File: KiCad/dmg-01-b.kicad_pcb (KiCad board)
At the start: 2 copper layers, 83 x 78.5 mm, 64 parts, among them CN1 SCREEN, CN2 CART, CN3 EXT, P1 GND PAD, P2 GND PAD, P3 GND PAD, P4 GND PAD, SW1 POWER_SW, U1 CPU, U2 VRAM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

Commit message: add images
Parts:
- G1: moved to F.Cu
- moved G1 32.7 mm to (38.3, 60.0), turned to 0 degrees
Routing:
- net GND: vias 138 -> 142
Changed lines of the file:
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@@
     )
   )
+  (footprint "eda-glyphs:kmc" (layer "F.Cu")
+    (at 38.3 60)
+    (property "Sheetfile" "dmg-01-b.kicad_sch")
+    (property "Sheetname" "")
+    (attr board_only exclude_from_pos_files)
+    (fp_text reference "G1" (at -0.254 -3.81) (layer "F.SilkS") hide
+      (effects (font (size 1.524 1.524) (thickness 0.3)))
+    )
+    (fp_text value "kmc" (at 0.75 0) (layer "F.SilkS") hide
+      (effects (font (size 1.524 1.524) (thickness 0.3)))
+    )
+    (fp_poly (pts
+        (xy -1.560389 -1.873672)
+        (xy -1.247107 -1.873672)
+        (xy -1.247107 -1.560389)
+        (xy -0.939849 -1.560389)
+        (xy -0.939849 -2.186954)
+        (xy -0.620541 -2.186954)
+        (xy -0.620541 -1.873672)
+        (xy -0.313283 -1.873672)
+        (xy -0.313283 -1.560389)
+        (xy 0 -1.560389)
+        (xy 0 -1.247106)
+        (xy 0.626565 -1.247106)
+        (xy 0.626565 -0.939848)
+        (xy 1.253131 -0.939848)
+        (xy 1.253131 -0.626566)
+        (xy 1.560389 -0.626566)
+        (xy 1.560389 -0.313283)
+        (xy 1.873671 -0.313283)
+        (xy 1.873671 0)
+        (xy 2.180929 0)
+        (xy 2.180929 -0.626566)
+        (xy 2.500237 -0.626566)
+        (xy 2.500237 0.006025)
+        (xy 2.186954 0.006025)
+        (xy 2.186954 0.319307)
+        (xy 1.873671 0.319307)
+        (xy 1.873671 0.939848)
+        (xy 1.566413 0.939848)
+        (xy 1.566413 2.186954)
+        (xy 1.247106 2.186954)
+        (xy 1.247106 1.879696)
+        (xy 0.933823 1.879696)
+        (xy 0.933823 1.566414)
+        (xy 0.626565 1.566414)
+        (xy 0.626565 2.186954)
+        (xy 0.307258 2.186954)
+        (xy 0.307258 1.879696)
+        (xy -0.006025 1.879696)
+        (xy -0.006025 1.566414)
+        (xy -0.620541 1.566414)
+        (xy -0.620541 1.879696)
+        (xy -0.933824 1.879696)
+        (xy -0.933824 2.186954)
+        (xy -1.253131 2.186954)
+        (xy -1.253131 1.566414)
+        (xy -1.560389 1.566414)
+        (xy -1.560389 1.879696)
+        (xy -1.879697 1.879696)
+        (xy -1.879697 0.626565)
+        (xy -2.186955 0.626565)
+        (xy -2.186955 0.319307)
+        (xy -2.500237 0.319307)
+        (xy -2.500237 -0.626566)
+        (xy -2.186955 -0.626566)
+        (xy -1.873672 -0.626566)
+        (xy -1.566414 -0.626566)
+        (xy -0.933824 -0.626566)
+        (xy -0.626566 -0.626566)
+        (xy -0.626566 -0.933824)
+        (xy -0.933824 -0.933824)
+        (xy -0.933824 -0.626566)
+        (xy -1.566414 -0.626566)
+        (xy -1.566414 -0.933824)
+        (xy -1.873672 -0.933824)
+        (xy -1.873672 -0.626566)
+        (xy -2.186955 -0.626566)
+        (xy -2.186955 -1.247106)
+        (xy -1.879697 -1.247106)
+        (xy -1.879697 -2.186954)
+        (xy -1.560389 -2.186954)
+      ) (layer "F.SilkS") (width 0) (fill solid))
+  )
   (footprint "Capacitor_SMD:C_0805_2012Metric_Pad1.18x1.45mm_HandSolder" (layer "F.Cu")
     (at 70 66.5)
@@
       (net 113 "-BATT") (pinfunction "BAT-") (pintype "passive"))
   )
-  (footprint "eda-glyphs:kmc" (layer "B.Cu")
-    (at 70.6 65.2 180)
-    (property "Sheetfile" "dmg-01-b.kicad_sch")
-    (property "Sheetname" "")
-    (attr board_only exclude_from_pos_files)
-    (fp_text reference "G1" (at -0.254 3.81) (layer "B.SilkS") hide
-      (effects (font (size 1.524 1.524) (thickness 0.3)) (justify mirror))
-    )
-    (fp_text value "kmc" (at 0.75 0) (layer "B.SilkS") hide
-      (effects (font (size 1.524 1.524) (thickness 0.3)) (justify mirror))
-    )
-    (fp_poly (pts
-        (xy -1.560389 1.873672)
-        (xy -1.247107 1.873672)
-        (xy -1.247107 1.560389)
-        (xy -0.939849 1.560389)
-        (xy -0.939849 2.186954)
-        (xy -0.620541 2.186954)
-        (xy -0.620541 1.873672)
-        (xy -0.313283 1.873672)
-        (xy -0.313283 1.560389)
-        (xy 0 1.560389)
-        (xy 0 1.247106)
-        (xy 0.626565 1.247106)
-        (xy 0.626565 0.939848)
-        (xy 1.253131 0.939848)
-        (xy 1.253131 0.626566)
-        (xy 1.560389 0.626566)
-        (xy 1.560389 0.313283)
-        (xy 1.873671 0.313283)
-        (xy 1.873671 0)
-        (xy 2.180929 0)
-        (xy 2.180929 0.626566)
-        (xy 2.500237 0.626566)
-        (xy 2.500237 -0.006025)
-        (xy 2.186954 -0.006025)
-        (xy 2.186954 -0.319307)
-        (xy 1.873671 -0.319307)
-        (xy 1.873671 -0.939848)
-        (xy 1.566413 -0.939848)
-        (xy 1.566413 -2.186954)
-        (xy 1.247106 -2.186954)
-        (xy 1.247106 -1.879696)
-        (xy 0.933823 -1.879696)
-        (xy 0.933823 -1.566414)
-        (xy 0.626565 -1.566414)
-        (xy 0.626565 -2.186954)
-        (xy 0.307258 -2.186954)
-        (xy 0.307258 -1.879696)
-        (xy -0.006025 -1.879696)
-        (xy -0.006025 -1.566414)
-        (xy -0.620541 -1.566414)
-        (xy -0.620541 -1.879696)
-        (xy -0.933824 -1.879696)
-        (xy -0.933824 -2.186954)
-        (xy -1.253131 -2.186954)
-        (xy -1.253131 -1.566414)
-        (xy -1.560389 -1.566414)
-        (xy -1.560389 -1.879696)
-        (xy -1.879697 -1.879696)
-        (xy -1.879697 -0.626565)
-        (xy -2.186955 -0.626565)
-        (xy -2.186955 -0.319307)
-        (xy -2.500237 -0.319307)
-        (xy -2.500237 0.626566)
-        (xy -2.186955 0.626566)
-        (xy -1.873672 0.626566)
-        (xy -1.566414 0.626566)
-        (xy -0.933824 0.626566)
-        (xy -0.626566 0.626566)
-        (xy -0.626566 0.933824)
-        (xy -0.933824 0.933824)
-        (xy -0.933824 0.626566)
-        (xy -1.566414 0.626566)
-        (xy -1.566414 0.933824)
-        (xy -1.873672 0.933824)
-        (xy -1.873672 0.626566)
-        (xy -2.186955 0.626566)
-        (xy -2.186955 1.247106)
-        (xy -1.879697 1.247106)
-        (xy -1.879697 2.186954)
-        (xy -1.560389 2.186954)
-      ) (layer "B.SilkS") (width 0) (fill solid))
-  )
   (footprint "kmc_lib:2.54_PAD_SMD_X7" (layer "B.Cu")
     (at 80.01 96.808 180)
@@
   (via (at 99.5 98) (size 0.8) (drill 0.4) (layers "F.Cu" "B.Cu") (free) (net 4))
   (via locked (at 64.5 95) (size 0.8) (drill 0.4) (layers "F.Cu" "B.Cu") (free) (net 4))
+  (via (at 44.5 59.5) (size 0.8) (drill 0.4) (layers "F.Cu" "B.Cu") (free) (net 4))
   (via (at 48.5 47.5) (size 0.8) (drill 0.4) (layers "F.Cu" "B.Cu") (free) (net 4))
   (via (at 93 46) (size 0.8) (drill 0.4) (layers "F.Cu" "B.Cu") (free) (net 4))
@@
   (via (at 58 53.3) (size 0.8) (drill 0.4) (layers "F.Cu" "B.Cu") (free) (net 4))
   (via (at 46.5 32.6) (size 0.8) (drill 0.4) (layers "F.Cu" "B.Cu") (free) (net 4))
+  (via (at 32 58) (size 0.8) (drill 0.4) (layers "F.Cu" "B.Cu") (free) (net 4))
   (via (at 66 41.2) (size 0.8) (drill 0.4) (layers "F.Cu" "B.Cu") (free) (net 4))
   (via locked (at 84 95) (size 0.8) (drill 0.4) (layers "F.Cu" "B.Cu") (free) (net 4))
@@
   (via locked (at 76.5 95) (size 0.8) (drill 0.4) (layers "F.Cu" "B.Cu") (free) (net 4))
   (via (at 60.3 36.3) (size 0.8) (drill 0.4) (layers "F.Cu" "B.Cu") (free) (net 4))
+  (via (at 32 62) (size 0.8) (drill 0.4) (layers "F.Cu" "B.Cu") (free) (net 4))
   (via (at 61.1 73.123522) (size 0.8) (drill 0.4) (layers "F.Cu" "B.Cu") (free) (net 4))
   (via locked (at 90 95) (size 0.8) (drill 0.4) (layers "F.Cu" "B.Cu") (free) (net 4))
@@
   (via (at 35.5 32.6) (size 0.8) (drill 0.4) (layers "F.Cu" "B.Cu") (free) (net 4))
   (via (at 62 49.2) (size 0.8) (drill 0.4) (layers "F.Cu" "B.Cu") (free) (net 4))
+  (via (at 44.5 63) (size 0.8) (drill 0.4) (layers "F.Cu" "B.Cu") (free) (net 4))
   (via (at 109 65) (size 0.8) (drill 0.4) (layers "F.Cu" "B.Cu") (free) (net 4))
   (via locked (at 87 95) (size 0.8) (drill 0.4) (layers "F.Cu" "B.Cu") (free) (net 4))
@@
     )
   )
-  (group "" (id ccebfcd8-a1f0-4a8e-b077-2c83658638a7)
-    (members
-      81ec17ae-7d6d-4574-af35-d4487429f438
-      8b992f09-a688-4516-ad0c-980240b33cef
-      cd2f768b-c470-48a2-84e0-481a100e3a25
-      eae9265d-2640-47e1-b8fe-024c47af79a6
-    )
-  )

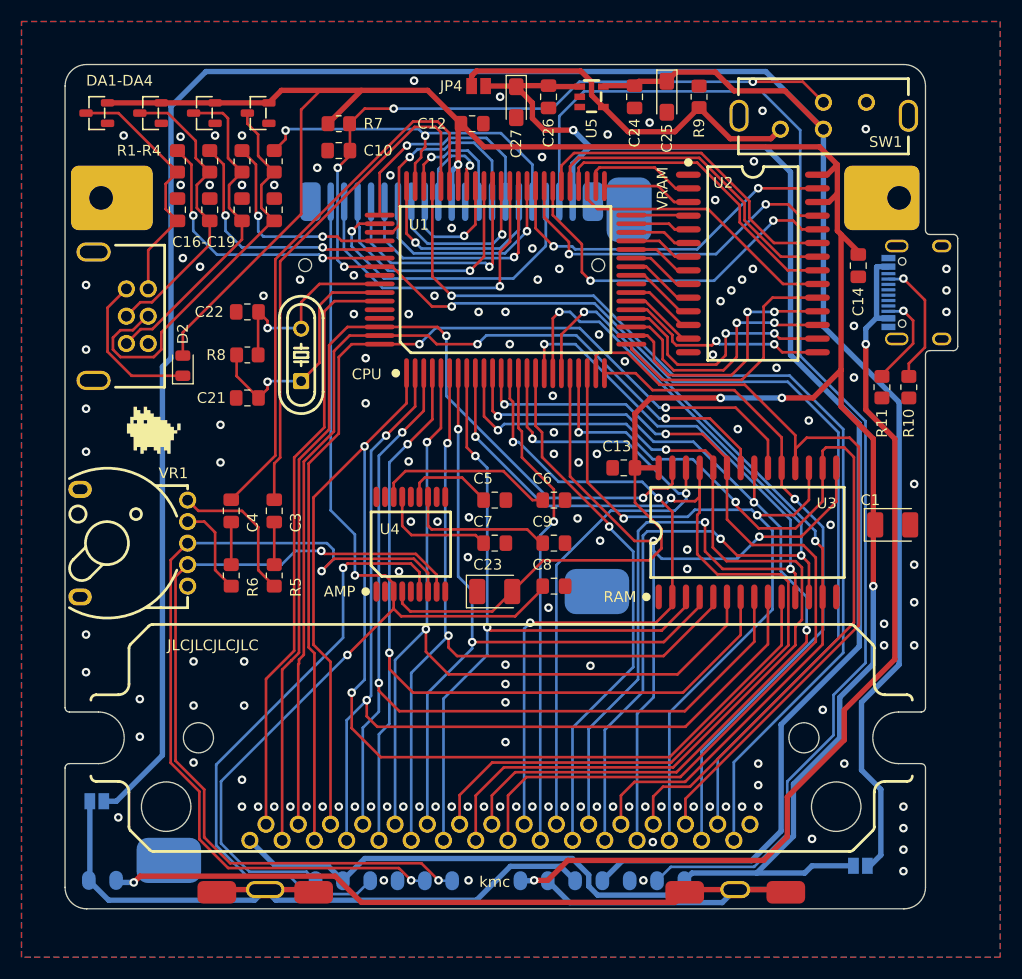
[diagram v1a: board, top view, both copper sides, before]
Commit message: - fix c23 orientation - fix d2 footprint - minor silkscreen changes
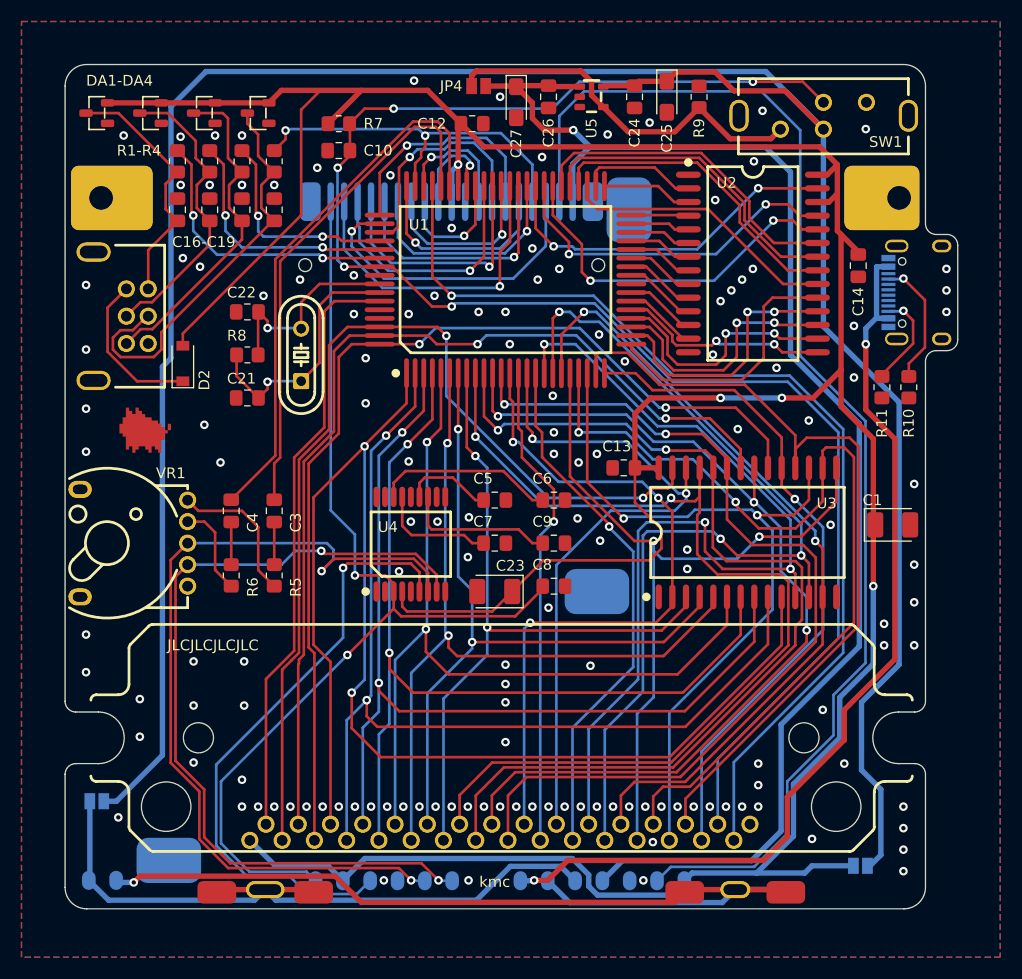
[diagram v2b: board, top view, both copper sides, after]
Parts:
- C23: value 100uf -> 100µf
- D2: value CD4148W -> 1N414; footprint Diode_SMD:D_0805_2012Metric -> Diode_SMD:D_SOD-123
- U5: footprint easyeda2kicad:SOT-23-5_L2.9-W1.6-P0.95-LS2.8-BL -> kmc_lib:SOT-23-5_L2.9-W1.6-P0.95-LS2.8-BL
- moved G1 0.58 mm to (37.8, 59.7)
- moved D2 0.20 mm to (41.0, 53.8)
- turned C23 to 180 degrees
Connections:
- C23 pad 1: GND -> +5V
- C23 pad 2: +5V -> GND
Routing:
- net +5V: track 320.1 -> 319.4 mm
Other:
- outline, holes or cut-outs redrawn

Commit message: remove extra power distribution switch capacitors since they were not needed
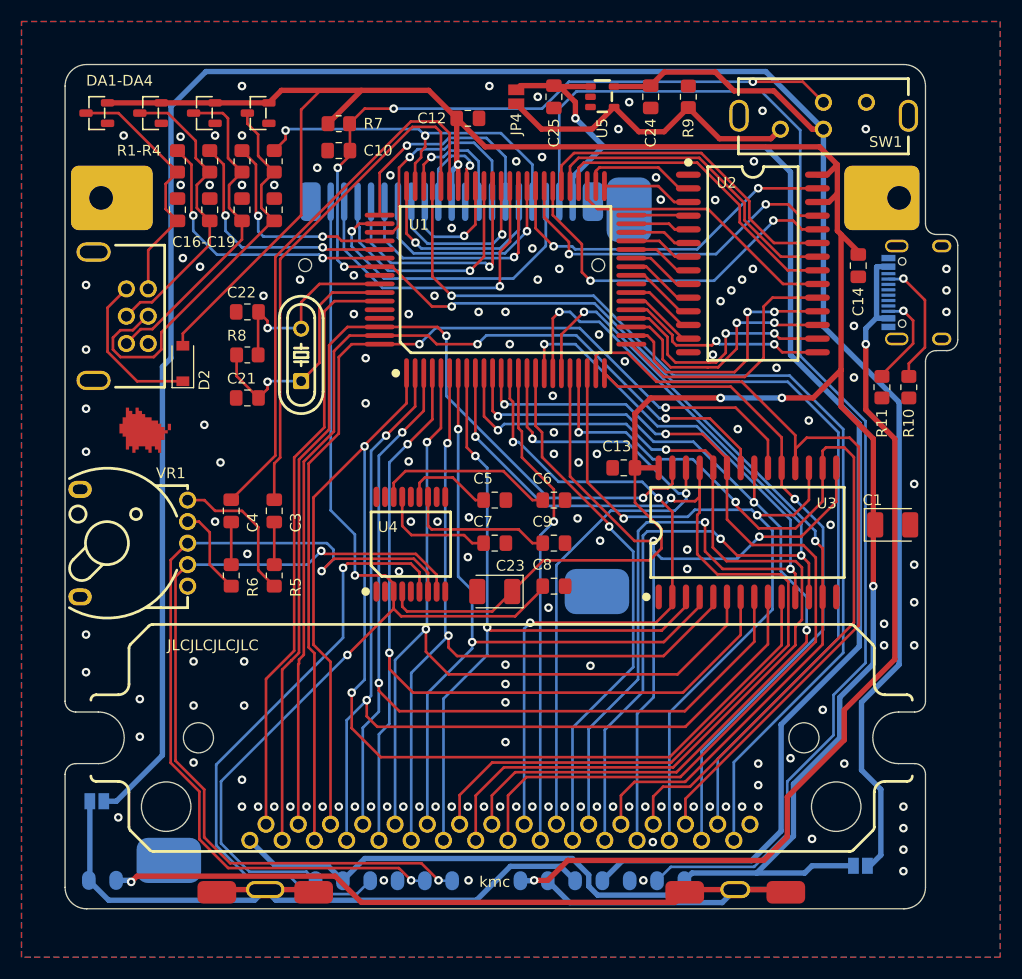
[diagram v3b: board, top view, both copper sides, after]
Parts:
- removed the C25 at (86.0, 29.0)
- removed C27: 22µf, Capacitor_Tantalum_SMD:CP_EIA-3216-18_Kemet-A_Pad1.58x1.35mm_HandSolder
- moved JP4 3.64 mm to (72.0, 29.0), turned to 90 degrees
- moved C24 1.50 mm to (84.5, 29.0)
- moved R9 1.00 mm to (88.0, 29.0)
- moved U5 1.00 mm to (80.0, 29.0)
- moved C12 0.64 mm to (67.5, 31.0)
- moved C25 0.50 mm to (75.5, 29.0)
- renumbered C26 to C25
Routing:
- net /SWITCH: track 35.4 -> 29.8 mm
- net +VSW: track 129.7 -> 125.2 mm
- net VIN: track 229.6 -> 228.6 mm
- net /MD5: track 23.8 -> 23.1 mm
- net GND: vias 142 -> 149

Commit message: update images
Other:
- board text added: "v1.3.1"
- board text removed: "v1.3"

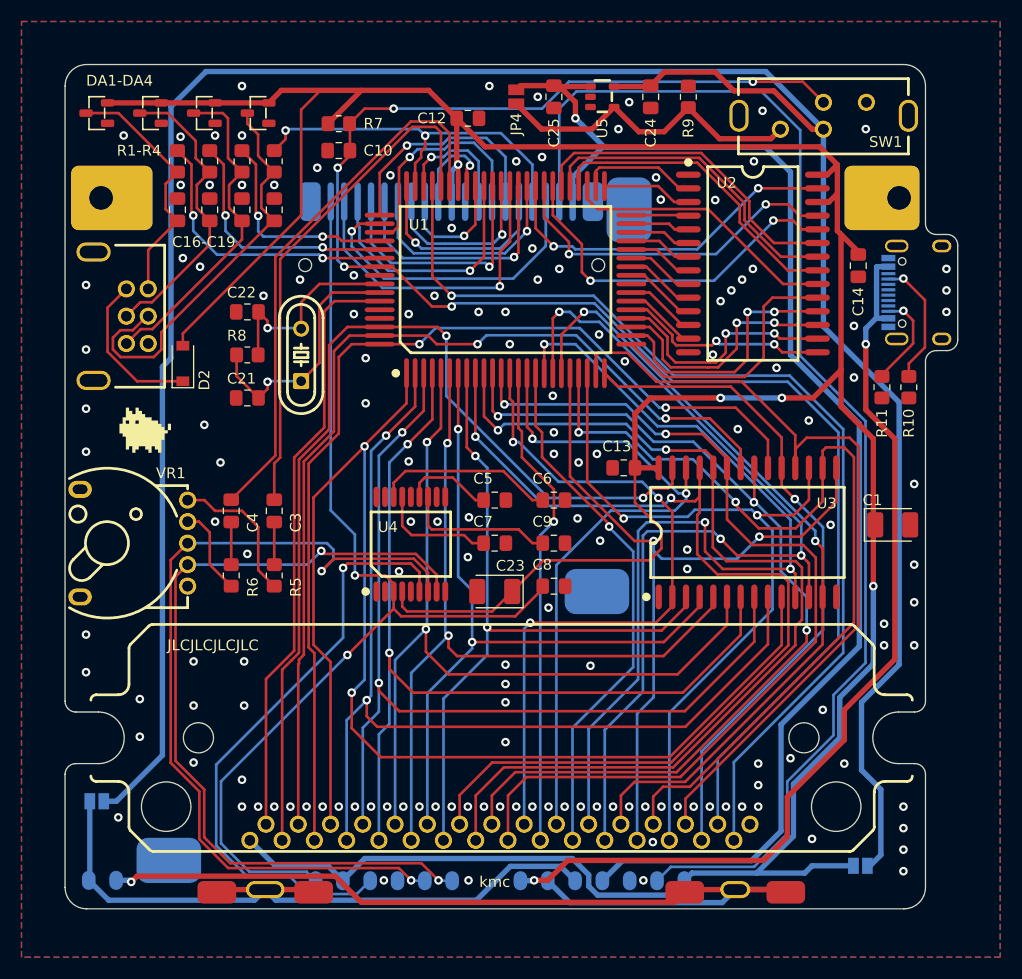
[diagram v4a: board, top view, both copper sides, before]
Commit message: remove unused SPKR pad clean up bottom area add optional jst style connectors
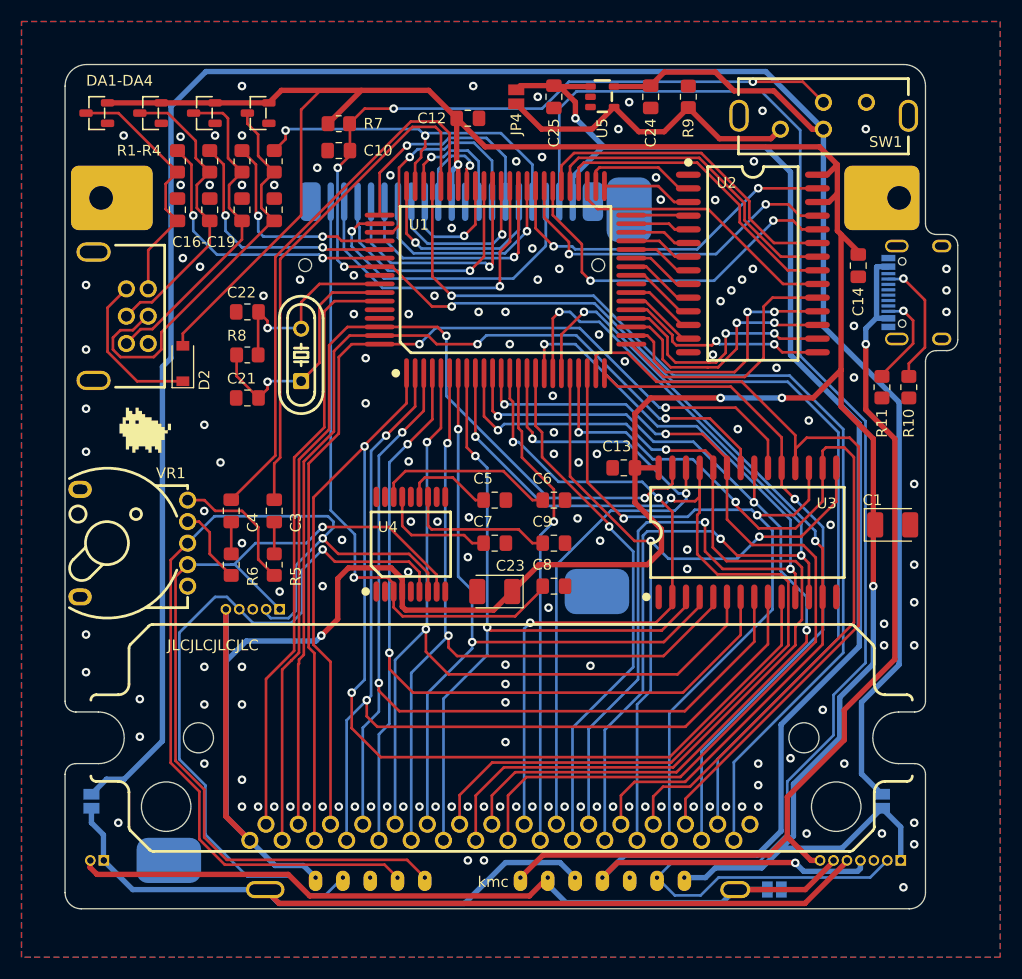
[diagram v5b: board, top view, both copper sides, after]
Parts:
- removed H4: AUX BATTERY HEADER, kmc_lib:2.54_PAD_SMD_X2
- added CN4: AUDIO, easyeda2kicad:CONN-TH_5P-P1.25_HCTL_HC-1.25-5AW, B.Cu at (47.5, 76.7)
- added CN5: POWER, easyeda2kicad:CONN-TH_7P-P1.25_HCTL_HC-1.25-7AW, B.Cu at (104.0, 100.0)
- added CN6: BATTERY, easyeda2kicad:CONN-TH_2P-P1.25_HCTL_HC-1.25-2AW, B.Cu at (33.0, 100.0)
- H2: value POWER HEADER -> POWER
- H3: value AUDIO HEADER -> AUDIO; footprint kmc_lib:2.54_PAD_SMD_X6 -> kmc_lib:2.54_PAD_SMD_X5
- moved JP2 6.32 mm to (106.0, 94.5), turned to -90 degrees
- moved H3 4.79 mm to (58.4, 101.6)
- moved JP3 1.00 mm to (96.0, 102.7)
- moved R5 1.00 mm to (49.5, 72.5)
- moved R6 1.00 mm to (45.5, 72.5)
- moved JP1 0.50 mm to (32.5, 94.5), turned to -90 degrees
- moved H2 0.29 mm to (80.0, 96.5)
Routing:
- net +BATT: track 65.3 -> 109.2 mm
- net /SPKR: track 96.1 -> 56.6 mm, vias 2 -> 1
- net +5V: track 319.8 -> 357.4 mm, vias 4 -> 5
- net +VSW: track 125.2 -> 150.2 mm, vias 1 -> 2
- net VEE: track 118.1 -> 141.4 mm
- net /AMP_EN: track 56.8 -> 68.0 mm
- net -BATT: track 86.9 -> 76.8 mm, vias 1 -> 0
- net /RPOT: track 80.8 -> 90.2 mm, vias 2 -> 1
- net VIN: track 228.6 -> 221.3 mm
- net /LPOT: track 77.8 -> 83.2 mm, vias 2 -> 1
- net VCC: track 87.4 -> 91.2 mm, vias 2 -> 1
- net /MD0: track 6.69 -> 4.73 mm
- net /RST: track 154.2 -> 152.5 mm
- net /P10: track 21.5 -> 20.4 mm
- net /MCS: track 25.9 -> 24.7 mm
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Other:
- outline, holes or cut-outs redrawn
- board text added: "B+"
- board text added: "B-"
- board text removed: "SPKR"
- board text removed: "VDD"
